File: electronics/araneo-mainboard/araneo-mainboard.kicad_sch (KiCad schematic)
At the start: 76 parts, among them J1 GPIO2, J2 OLED, J3 GPIO1, SW2 SW, SW3 SW, U1 IMU, U3 TLV1117-ADJ, U4 POWER, U5 PAM8403D

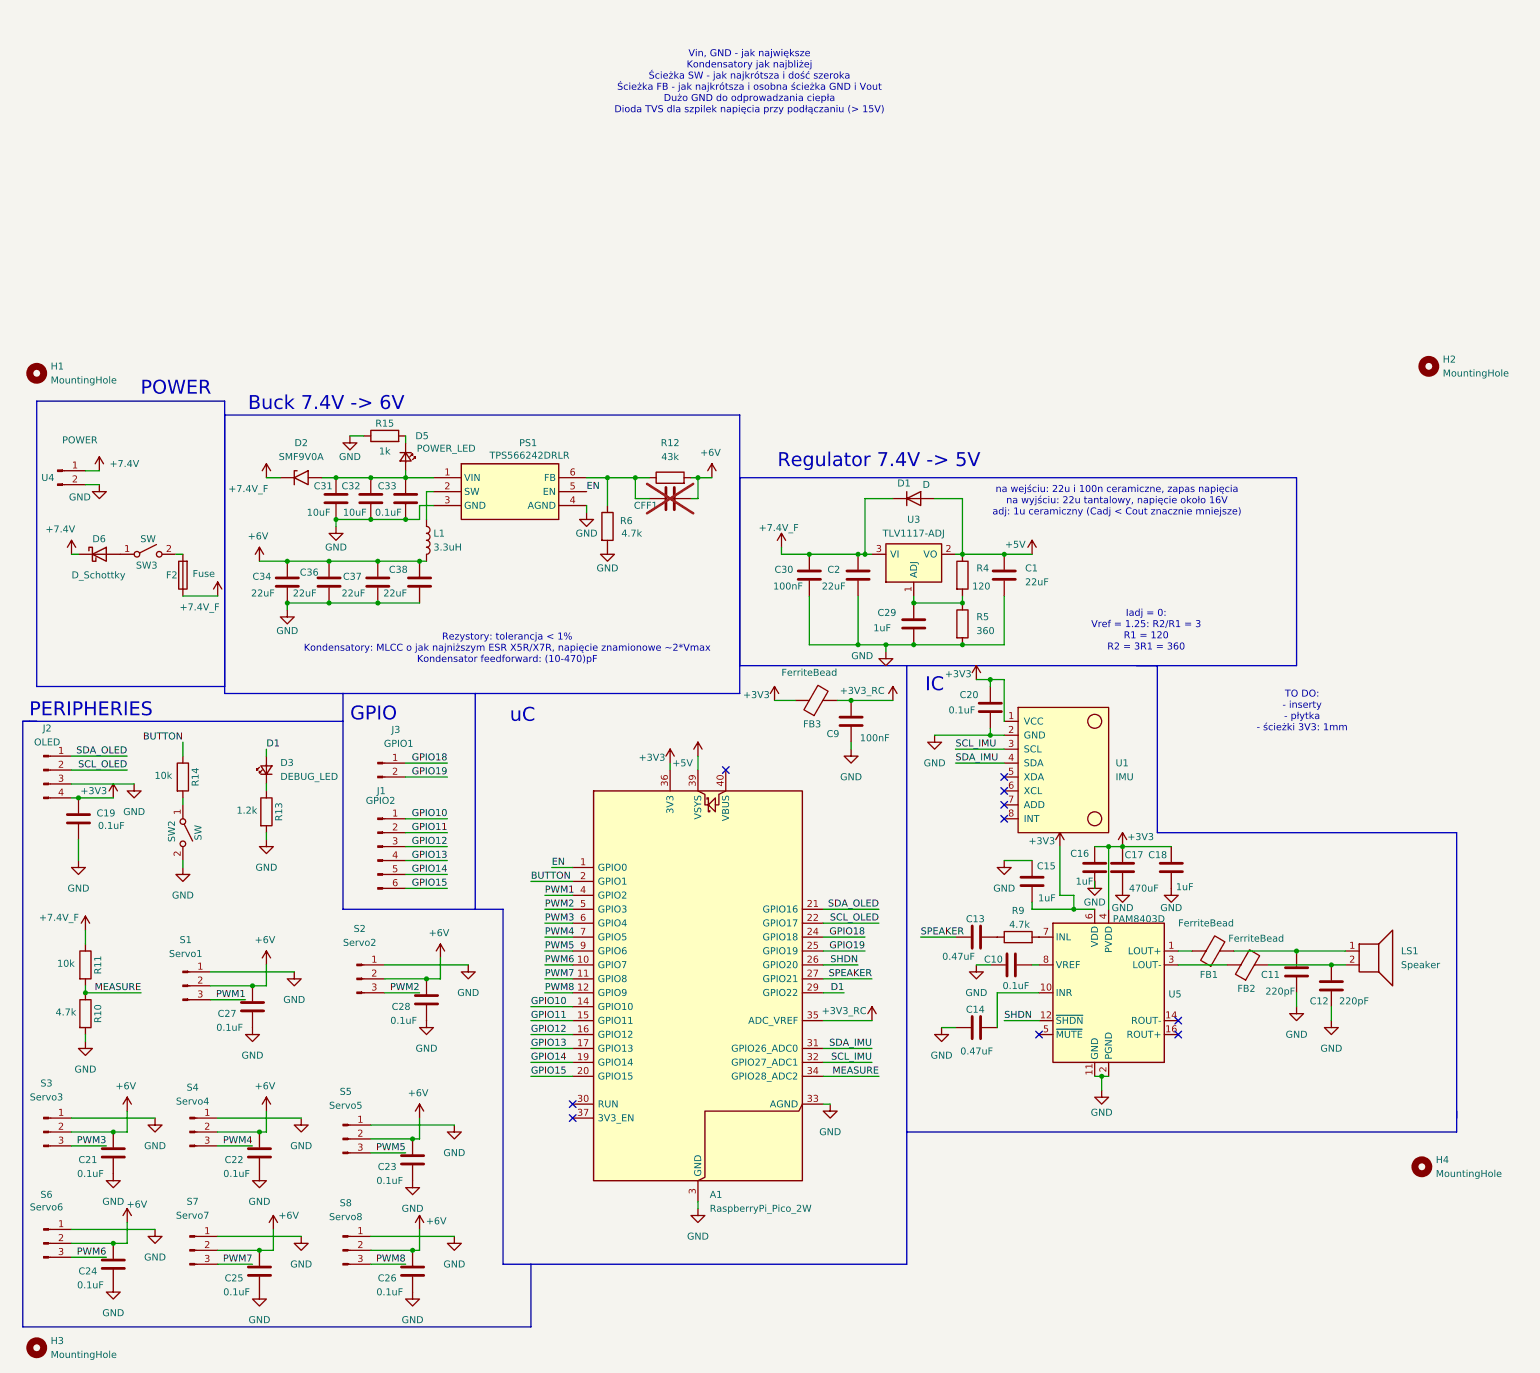
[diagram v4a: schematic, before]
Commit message: electronics: add bmi270 and second buck
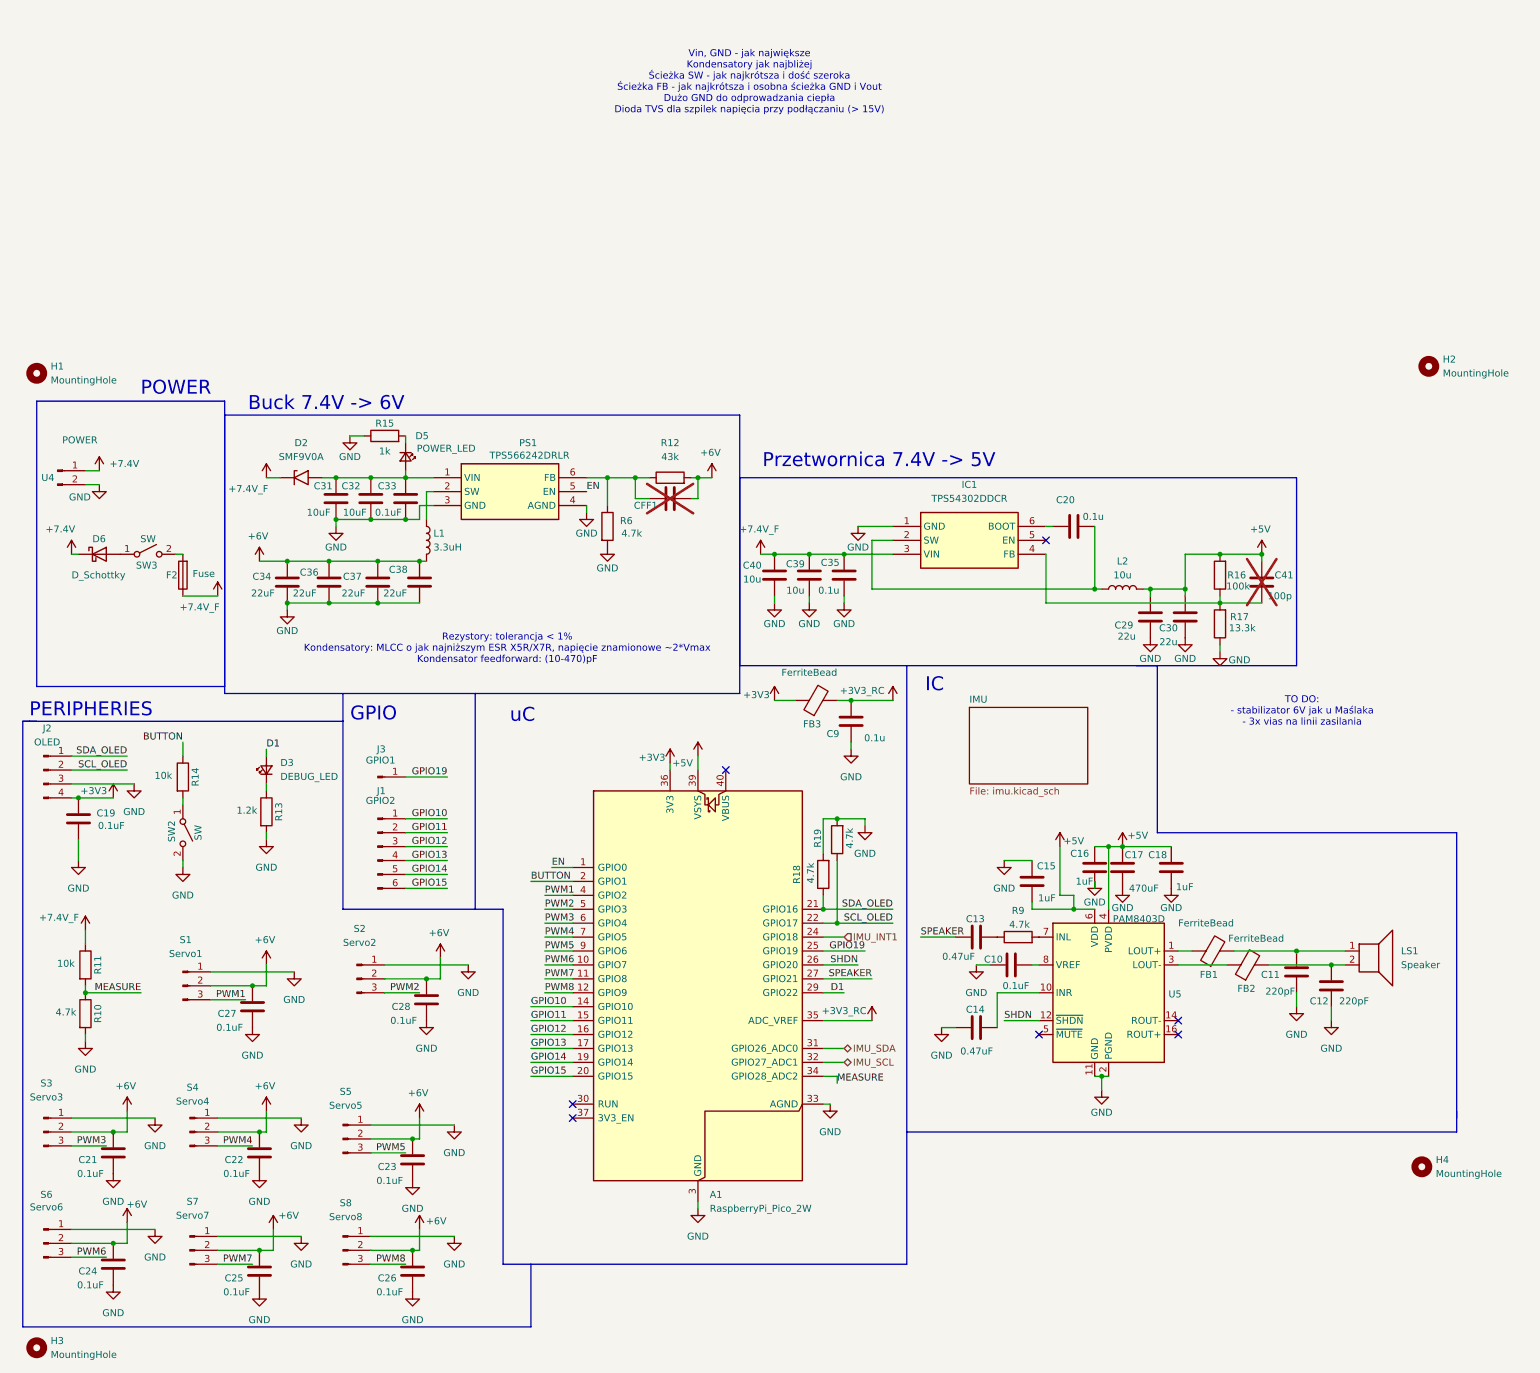
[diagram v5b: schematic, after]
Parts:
- removed C1: 22uF, Capacitor_Tantalum_SMD:CP_EIA-3528-15_AVX-H_HandSolder, symbol Device:C
- removed C2: 22uF, Capacitor_SMD:C_1210_3225Metric_Pad1.33x2.70mm_HandSolder, symbol Device:C
- removed D1: D, Diode_THT:D_DO-41_SOD81_P10.16mm_Horizontal, symbol Device:D
- removed J3: GPIO1, Connector_PinHeader_2.54mm:PinHeader_1x02_P2.54mm_Vertical, symbol Connector:Conn_01x02_Pin
- removed R4: 120, Resistor_SMD:R_0603_1608Metric_Pad0.98x0.95mm_HandSolder, symbol Device:R
- removed R5: 360, Resistor_SMD:R_0603_1608Metric_Pad0.98x0.95mm_HandSolder, symbol Device:R
- removed U1: IMU, usini_sensors:module_mpu6050, symbol Usini:module_mpu6050
- removed U3: TLV1117-ADJ, Package_TO_SOT_SMD:SOT-223-3_TabPin2, symbol Regulator_Linear:TLV1117-ADJ
- added C35: 0.1u, Capacitor_SMD:C_0603_1608Metric_Pad1.08x0.95mm_HandSolder, symbol Device:C
- added C39, C40: 10u, Capacitor_SMD:C_1206_3216Metric_Pad1.33x1.80mm_HandSolder, symbol Device:C
- added C41: 100p, Capacitor_SMD:C_0603_1608Metric_Pad1.08x0.95mm_HandSolder, symbol Device:C
- added IC1: TPS54302DDCR, custom_footprints:SOT95P280X110-6N, symbol Symbols:TPS54302DDCR
- added J3: GPIO1, Connector_PinHeader_2.54mm:PinHeader_1x01_P2.54mm_Vertical, symbol Connector:Conn_01x01_Pin
- added L2: 10u, custom_footprints:PA4302103NLT, symbol Device:L
- added R16: 100k, Resistor_SMD:R_0603_1608Metric_Pad0.98x0.95mm_HandSolder, symbol Device:R
- added R17: 13.3k, Resistor_SMD:R_0603_1608Metric_Pad0.98x0.95mm_HandSolder, symbol Device:R
- added R18, R19: 4.7k, Resistor_SMD:R_0603_1608Metric_Pad0.98x0.95mm_HandSolder, symbol Device:R
- C20: value 0.1uF -> 0.1u
- C29: value 1uF -> 22u; footprint Capacitor_SMD:C_0603_1608Metric_Pad1.08x0.95mm_HandSolder -> Capacitor_SMD:C_0805_2012Metric_Pad1.18x1.45mm_HandSolder
- C30: value 100nF -> 22u; footprint Capacitor_SMD:C_0603_1608Metric_Pad1.08x0.95mm_HandSolder -> Capacitor_SMD:C_0805_2012Metric_Pad1.18x1.45mm_HandSolder
- C34, C36, C37, C38: footprint Capacitor_SMD:C_1210_3225Metric_Pad1.33x2.70mm_HandSolder -> Capacitor_SMD:C_0805_2012Metric_Pad1.18x1.45mm_HandSolder
- C9: value 100nF -> 0.1u
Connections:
- net +3V3: no longer C15.1, C16.2, C17.2, C18.2, C20.1, U5.13 (PVDD), U5.4 (PVDD), U5.6 (VDD)
- net +5V: now also C15.1, C16.2, C17.2, C18.2, C29.1, C30.1, U5.13 (PVDD), U5.4 (PVDD), U5.6 (VDD), C41.1, L2.2, R16.2
- net +7.4V_F: now also C35.1, C39.1, C40.1, IC1.3 (VIN); no longer C30.1
- net GND: now also C35.2, C39.2, C40.2, IC1.1 (GND), R17.1, R18.2, R19.2; no longer C20.2
- net GPIO19: now also J3.1 (Pin_1)
- net SCL_OLED: now also R19.1
- net SDA_OLED: now also R18.1
- net GPIO18 renamed IMU_INT1
- net SCL_IMU renamed IMU_SCL
- net SDA_IMU renamed IMU_SDA
- new net: C20.1, IC1.2 (SW), L2.1
- new net: C20.2, IC1.6 (BOOT)
- new net: C41.2, IC1.4 (FB), R16.1, R17.2
- no-connect marks 10 -> 7
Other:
- added sheet IMU (imu.kicad_sch)
- note added: "Przetwornica 7.4V -> 5V"
- note added: "TO DO: - stabilizator 6V jak u Maślaka - 3x vias na linii zasilania"
- note removed: "Iadj = 0: Vref = 1.25: R2/R1 = 3 R1 = 120 R2 = 3R1 = 360"
- note removed: "Regulator 7.4V -> 5V"
- note removed: "TO DO: - inserty - płytka - ścieżki 3V3: 1mm"
- note removed: "na wejściu: 22u i 100n ceramiczne, zapas napięcia na wyjściu: 22u tantalowy, napięcie około 16V adj: 1u ceramiczny (Cadj < Cout znacznie mniejsze)"

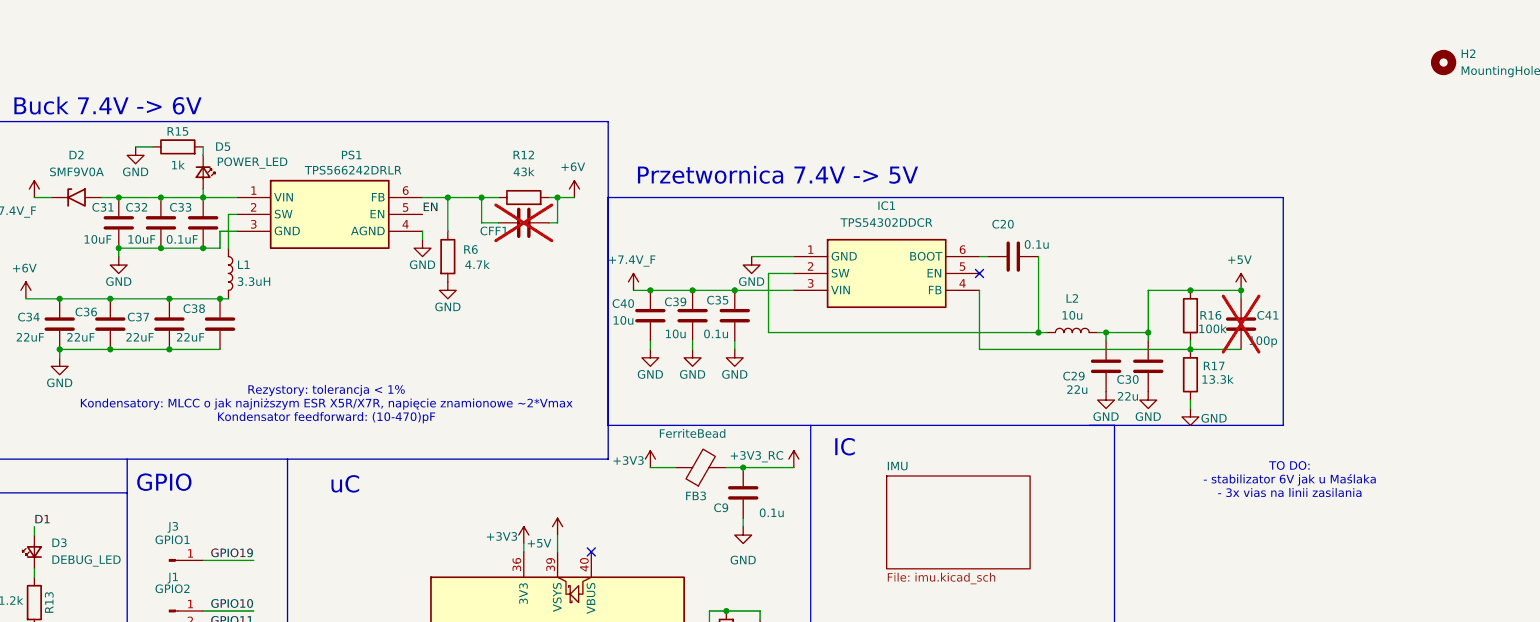
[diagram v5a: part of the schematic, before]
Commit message: electronics: add diode indicator
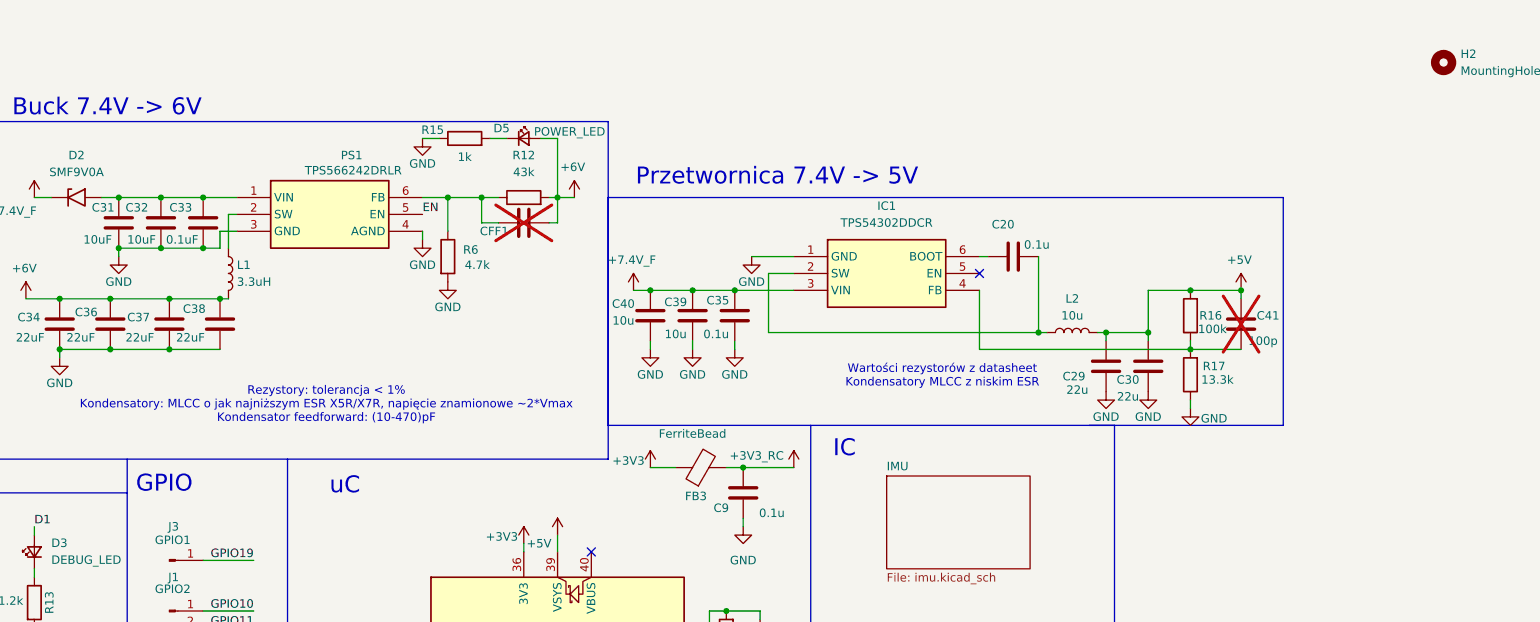
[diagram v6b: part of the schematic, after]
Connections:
- net +6V: now also D5.2 (A)
- net at C31.1, C32.1, C33.1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: no longer D5.2 (A)
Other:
- note added: "Wartości rezystorów z datasheet Kondensatory MLCC z niskim ESR"
- note removed: "TO DO: - stabilizator 6V jak u Maślaka - 3x vias na linii zasilania"
